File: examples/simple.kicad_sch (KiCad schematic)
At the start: 78 parts, among them J1 Conn_02x10_Odd_Even, U1 OPA145ID, U2 CD4053B, U3 OPA172ID, U4 OPA145ID, U5 OPA172ID, U6 LM4040DBZ-5, U7 OP07, U8 NE5534, U9 OP07

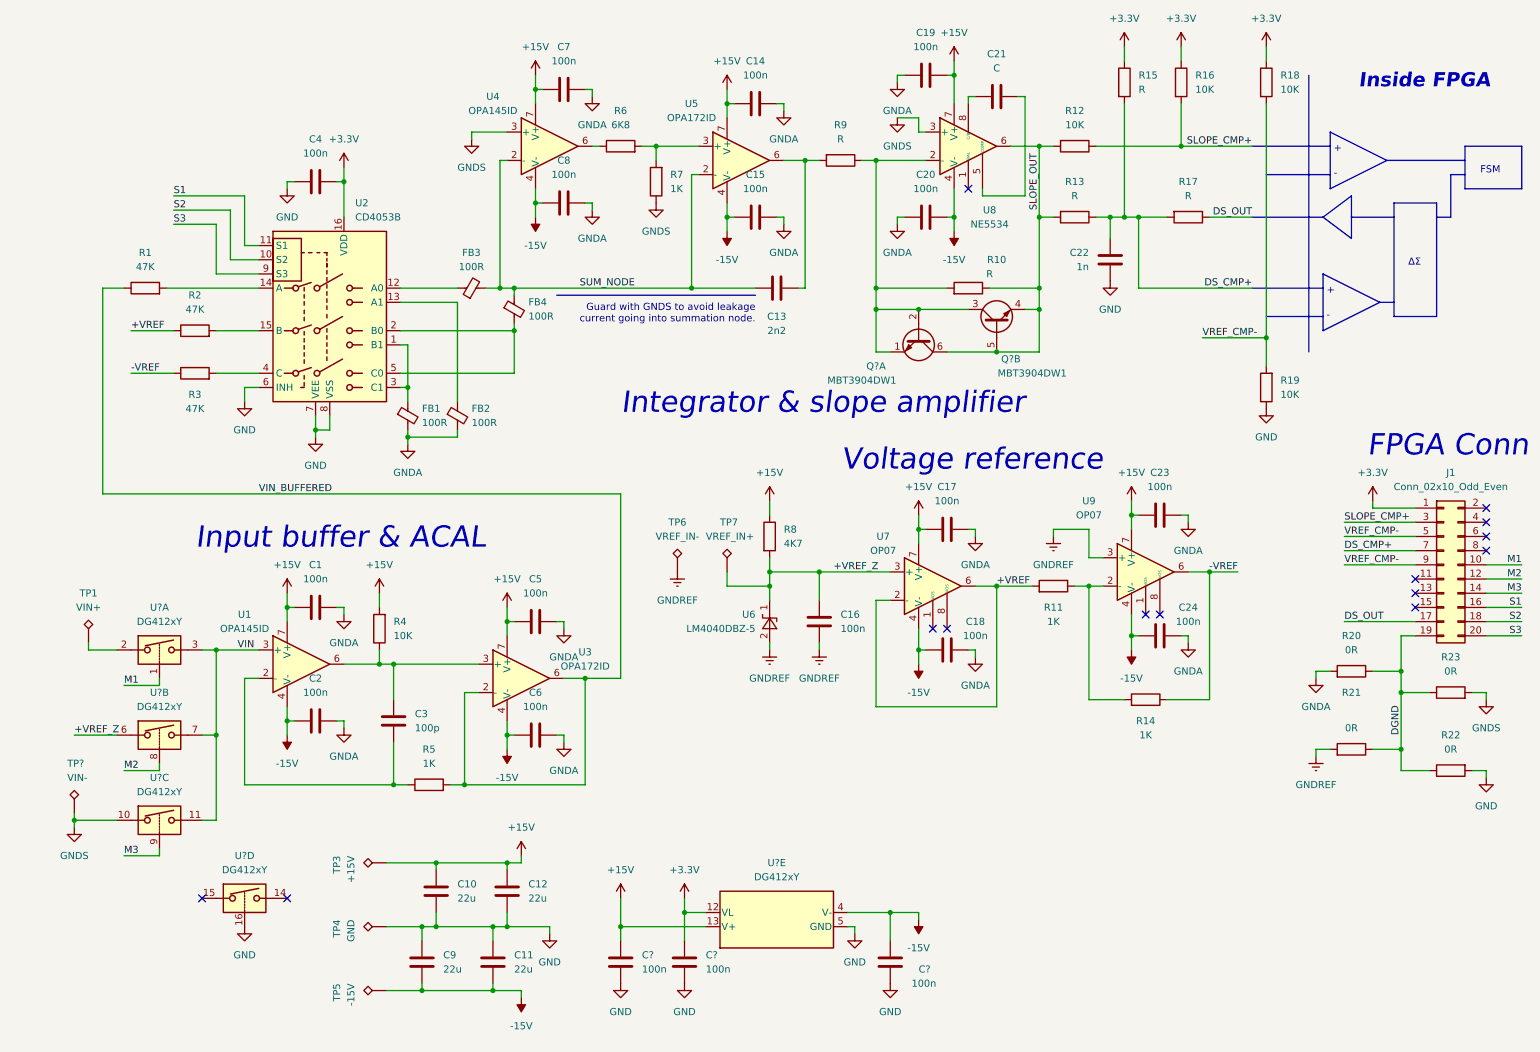
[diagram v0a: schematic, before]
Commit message: Started layout
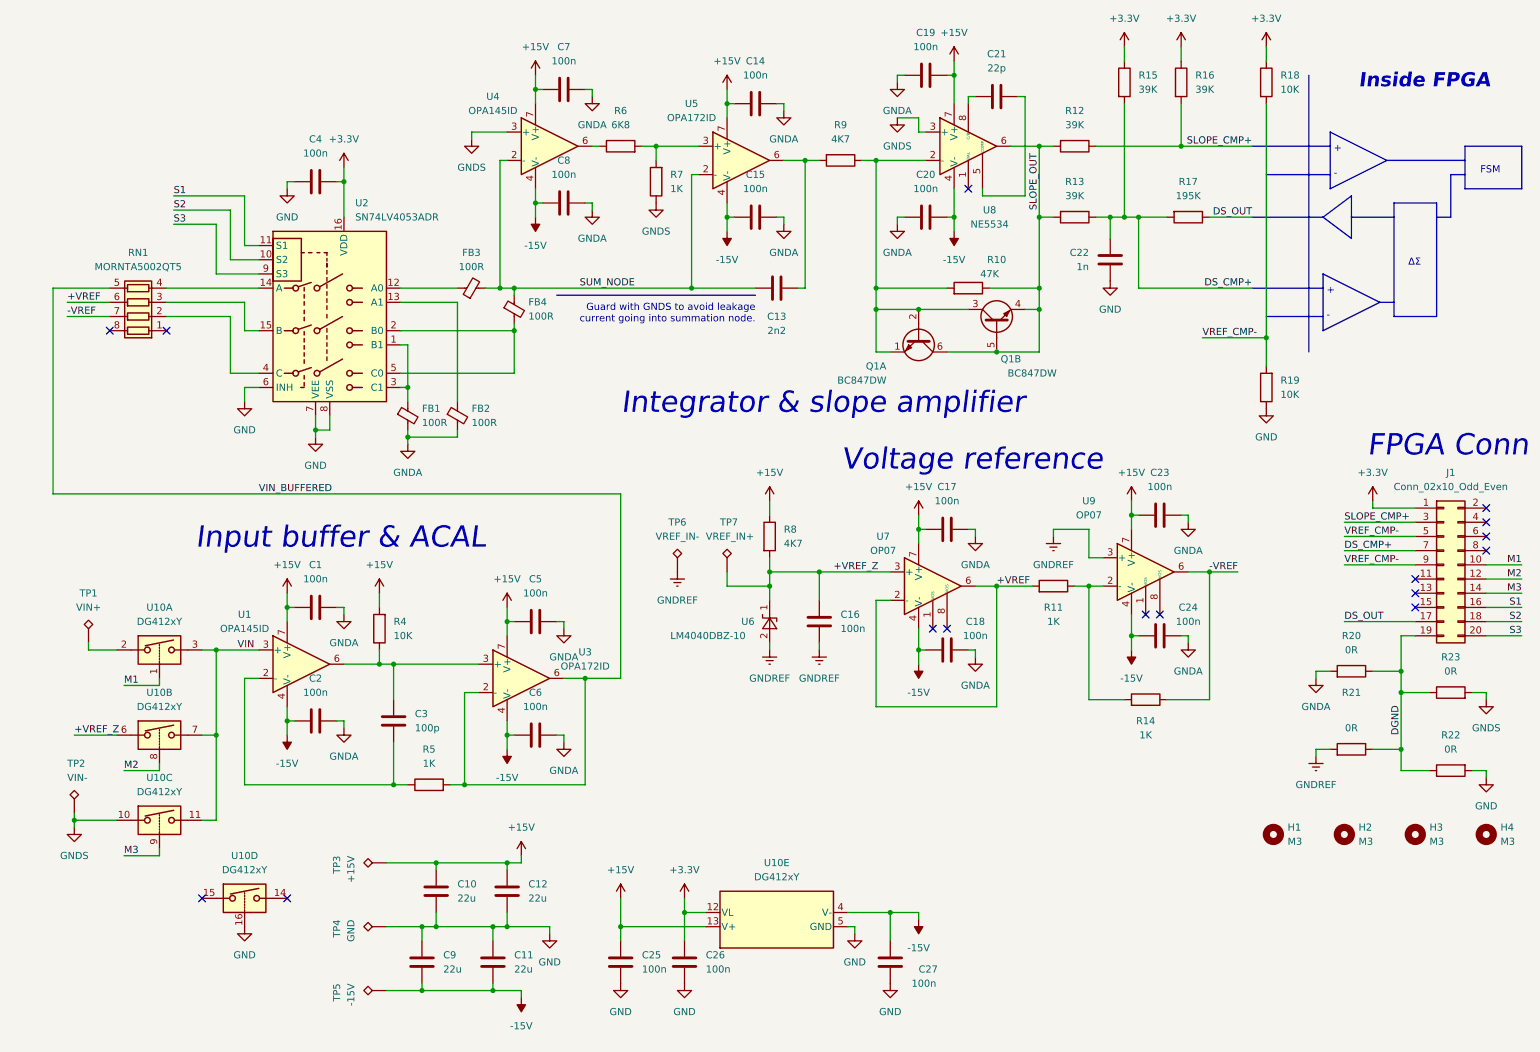
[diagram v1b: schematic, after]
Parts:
- removed R1, R2, R3: 47K, Resistor_SMD:R_0805_2012Metric_Pad1.20x1.40mm_HandSolder, symbol Device:R
- added H1, H2, H3, H4: M3, MountingHole:MountingHole_3.2mm_M3, symbol Mechanical:MountingHole
- added RN1: MORNTA5002QT5, Package_SO:MSOP-8_3x3mm_P0.65mm, symbol Device:R_Pack04
- C21: value C -> 22p
- Q1: renamed from Q?; value MBT3904DW1 -> BC847DW; #mouser (none) -> 863-SBC847BPDW1T1G
- R10: value R -> 47K
- R12, R16: value 10K -> 39K
- R13, R15: value R -> 39K
- R17: value R -> 195K
- R9: value R -> 4K7
- U1, U4: #mouser (none) -> 595-OPA145IDR
- U10: renamed from U?; #mouser (none) -> 781-DG412DY-T1-E3
- U2: value CD4053B -> SN74LV4053ADR; #mouser (none) -> 595-SN74LV4053ADR
- U3, U5: #mouser (none) -> 595-OPA172IDR
- U6: value LM4040DBZ-5 -> LM4040DBZ-10
- U7, U9: #mouser (none) -> 595-OP07CDR
- U8: #mouser (none) -> 595-NE5534AD
- gave numbers to parts that had none: 4
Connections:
- net +VREF: now also RN1.6 (R3.2)
- net -VREF: now also RN1.7 (R2.2)
- net VIN_BUFFERED: now also RN1.5 (R4.2)
- net at U2.14 (A): now also RN1.4 (R4.1)
- net at U2.15 (B): now also RN1.3 (R3.1)
- net at U2.4 (C): now also RN1.2 (R2.1)
- no-connect marks 14 -> 16

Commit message: Changed footprints in schematic
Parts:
- C22, C3: footprint Capacitor_SMD:C_0805_2012Metric_Pad1.18x1.45mm_HandSolder -> Capacitor_SMD:C_0603_1608Metric_Pad1.08x0.95mm_HandSolder
- R10, R11, R12, R13, R14, R15, R16, R17, R18, R19, R20, R21, R22, R23, R4, R5, R6, R7, R8, R9: footprint Resistor_SMD:R_0805_2012Metric_Pad1.20x1.40mm_HandSolder -> Resistor_SMD:R_0603_1608Metric_Pad0.98x0.95mm_HandSolder

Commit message: Layout work
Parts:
- added C?: 100n, Capacitor_SMD:C_0402_1005Metric_Pad0.74x0.62mm_HandSolder, symbol Device:C
- added Q2: MMBT3904, Package_TO_SOT_SMD:SOT-23, symbol Transistor_BJT:MMBT3904
- added R1: 10K, Resistor_SMD:R_0603_1608Metric_Pad0.98x0.95mm_HandSolder, symbol Device:R
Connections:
- net +15V: now also R1.2
- net +VREF_Z: now also U10.10; no longer U10.6
- net GND: no longer U10.16, U2.6 (INH)
- net GNDA: now also RN1.1 (R1.1), U2.6 (INH)
- net GNDS: now also U10.6, U4.1 (NC), U5.1 (NC), U5.8 (NC), C?.1, Q2.2 (E); no longer U10.10
- net M2: now also U10.9; no longer U10.8
- net M3: now also U10.8; no longer U10.9
- net VIN: now also U10.14
- net at U10.15: now also C?.2, Q2.1 (B), Q2.3 (C), R1.1
- net at RN1.2 (R2.1): now also U2.15 (B); no longer U2.4 (C)
- net at RN1.3 (R3.1): now also U2.4 (C); no longer U2.15 (B)
- new net M4: U10.16
- no-connect marks 16 -> 13
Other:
- moved on the sheet: C15, C8, TP2, U10A, U10B, U10C, U10D

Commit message: Layout work
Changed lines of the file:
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@@
   )
   (text "Guard with GNDS to avoid leakage \ncurrent going into summation node."
-    (at 142.24 69.85 0)
+    (at 142.24 69.85 180)
     (effects (font (size 1.27 1.27)) (justify right bottom))
   )
@@
       (effects (font (size 1.27 1.27)) hide)
     )
+    (pin "1")
+    (pin "2")
+    (pin "6")
     (pin "3")
     (pin "4")
@@
       (effects (font (size 1.27 1.27)) hide)
     )
+    (pin "1")
+    (pin "2")
+    (pin "3")
+    (pin "6")
+    (pin "7")
+    (pin "8")
+    (pin "10")
+    (pin "11")
+    (pin "9")
     (pin "14")
     (pin "15")
     (pin "16")
+    (pin "12")
+    (pin "13")
+    (pin "4")
+    (pin "5")
   )
   (symbol (lib_id "Device:R") (at 248.92 146.05 270) (mirror x) (unit 1)
     (in_bom yes) (on_board yes)
-    (property "Reference" "R21" (id 0) (at 248.92 135.89 90))
+    (property "Reference" "R21" (id 0) (at 248.92 139.7 90))
     (property "Value" "0R" (id 1) (at 248.92 142.24 90))
     (property "Footprint" "Resistor_SMD:R_0603_1608Metric_Pad0.98x0.95mm_HandSolder" (id 2) (at 248.92 147.828 90)
@@
       (effects (font (size 1.27 1.27)) hide)
     )
+    (pin "1")
+    (pin "2")
+    (pin "3")
+    (pin "6")
+    (pin "7")
+    (pin "8")
     (pin "10")
     (pin "11")
     (pin "9")
+    (pin "14")
+    (pin "15")
+    (pin "16")
+    (pin "12")
+    (pin "13")
+    (pin "4")
+    (pin "5")
   )
   (symbol (lib_id "power:GNDA") (at 242.57 133.35 0) (unit 1)
@@
       (effects (font (size 1.27 1.27)) hide)
     )
+    (pin "1")
+    (pin "2")
+    (pin "3")
     (pin "6")
     (pin "7")
     (pin "8")
+    (pin "10")
+    (pin "11")
+    (pin "9")
+    (pin "14")
+    (pin "15")
+    (pin "16")
+    (pin "12")
+    (pin "13")
+    (pin "4")
+    (pin "5")
   )
   (symbol (lib_id "power:GNDS") (at 22.86 160.02 0) (unit 1)
@@
     (pin "2")
     (pin "6")
+    (pin "3")
+    (pin "4")
+    (pin "5")
   )
   (symbol (lib_id "power:GNDA") (at 219.71 105.41 0) (unit 1)
@@
       (effects (font (size 1.27 1.27)) hide)
     )
+    (pin "1")
+    (pin "2")
+    (pin "3")
+    (pin "6")
+    (pin "7")
+    (pin "8")
+    (pin "10")
+    (pin "11")
+    (pin "9")
+    (pin "14")
+    (pin "15")
+    (pin "16")
     (pin "12")
     (pin "13")
@@
     (pin "2")
     (pin "3")
+    (pin "6")
+    (pin "7")
+    (pin "8")
+    (pin "10")
+    (pin "11")
+    (pin "9")
+    (pin "14")
+    (pin "15")
+    (pin "16")
+    (pin "12")
+    (pin "13")
+    (pin "4")
+    (pin "5")
   )
   (symbol (lib_id "power:+15V") (at 137.16 27.94 0) (unit 1)

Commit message: Finished layout
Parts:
- removed R21: 0R, Resistor_SMD:R_0603_1608Metric_Pad0.98x0.95mm_HandSolder, symbol Device:R
- added NT1: NetTie_2, NetTie:NetTie-2_SMD_Pad0.5mm, symbol Device:NetTie_2
- TP1, TP2, TP3, TP4, TP5, TP6, TP7: now left out of the parts list
- gave numbers to parts that had none: 1
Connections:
- net DGND: no longer R23.1
- net GNDA: now also NT1.1
- net GNDREF: now also R23.1, NT1.2
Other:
- moved on the sheet: C16, R23
